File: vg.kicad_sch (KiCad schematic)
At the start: 45 parts, among them J1 Conn_01x07, J2 Conn_01x08, J3 Conn_01x03, Q1 2N7002, Q3 SI2301CDS-T1-GE3, U1 TPS62203DBV, U2 IRLML6344TRPBF, U3 STM32L072CBTx, Y1 32768Hz - 12,5 pF

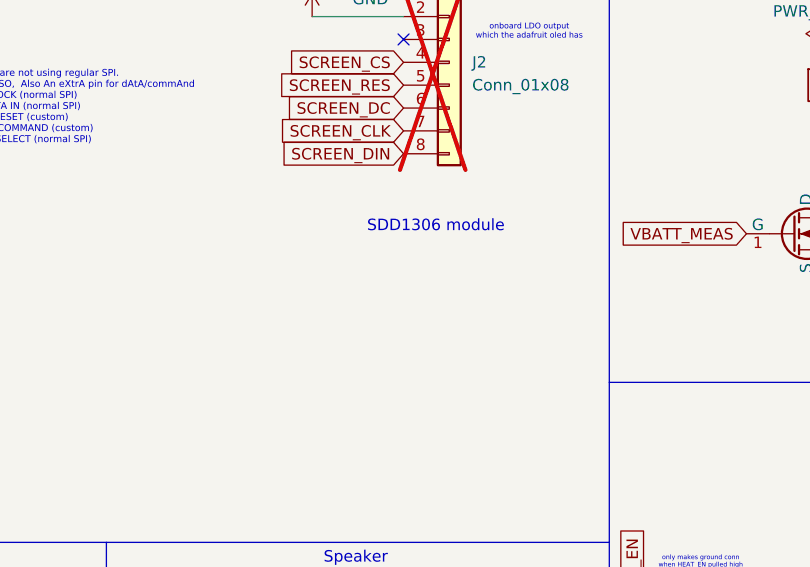
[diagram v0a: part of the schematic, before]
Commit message: add 2nd pin row
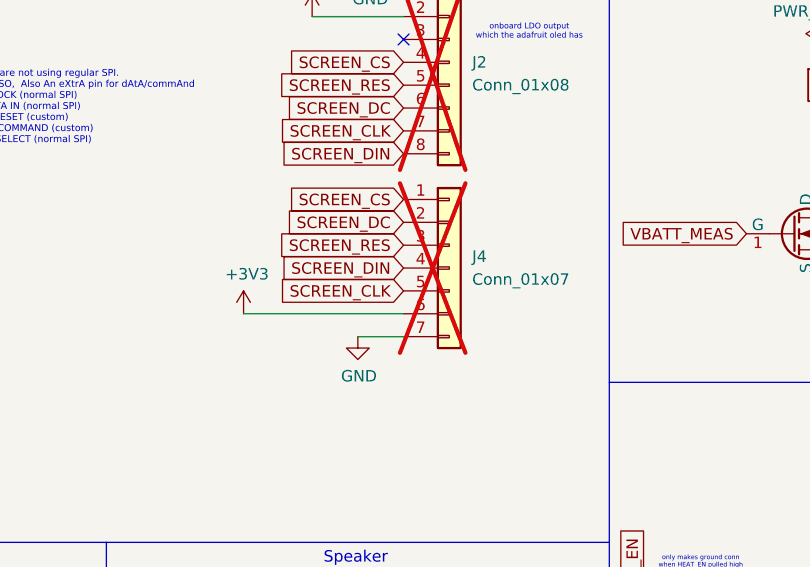
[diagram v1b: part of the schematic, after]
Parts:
- added J4: Conn_01x07, Connector_PinHeader_2.54mm:PinHeader_1x07_P2.54mm_Vertical, symbol Connector_Generic:Conn_01x07
- J2: footprint Connector_PinHeader_2.54mm:PinHeader_1x08_P2.54mm_Horizontal -> Connector_PinHeader_2.54mm:PinHeader_1x08_P2.54mm_Vertical
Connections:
- net +3V3: now also J4.6 (Pin_6)
- net GND: now also J4.7 (Pin_7)
- net SCREEN_CLK: now also J4.5 (Pin_5)
- net SCREEN_CS: now also J4.1 (Pin_1)
- net SCREEN_DC: now also J4.2 (Pin_2)
- net SCREEN_DIN: now also J4.4 (Pin_4)
- net SCREEN_RES: now also J4.3 (Pin_3)
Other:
- note removed: "SDD1306 module"

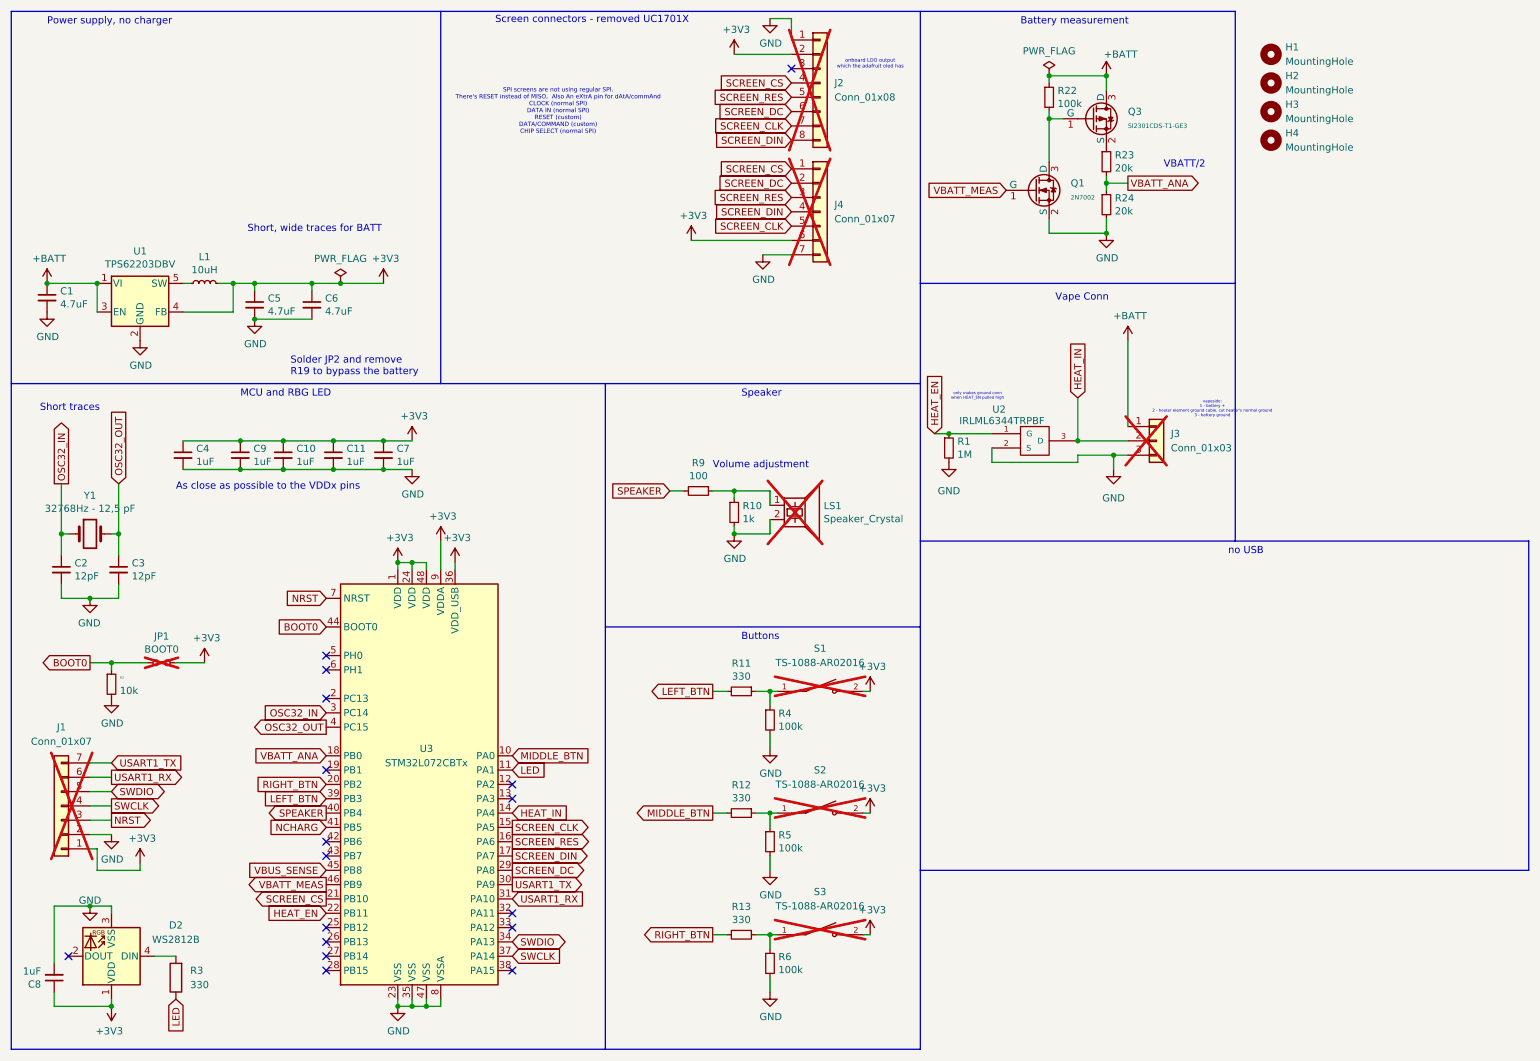
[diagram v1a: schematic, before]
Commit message: dont pour all the way to the edge; replace speaker series cap with 0805 for better thermal; gnd vias on both sides of islands; long trace series resistors close to chip; shorter filter cap connections
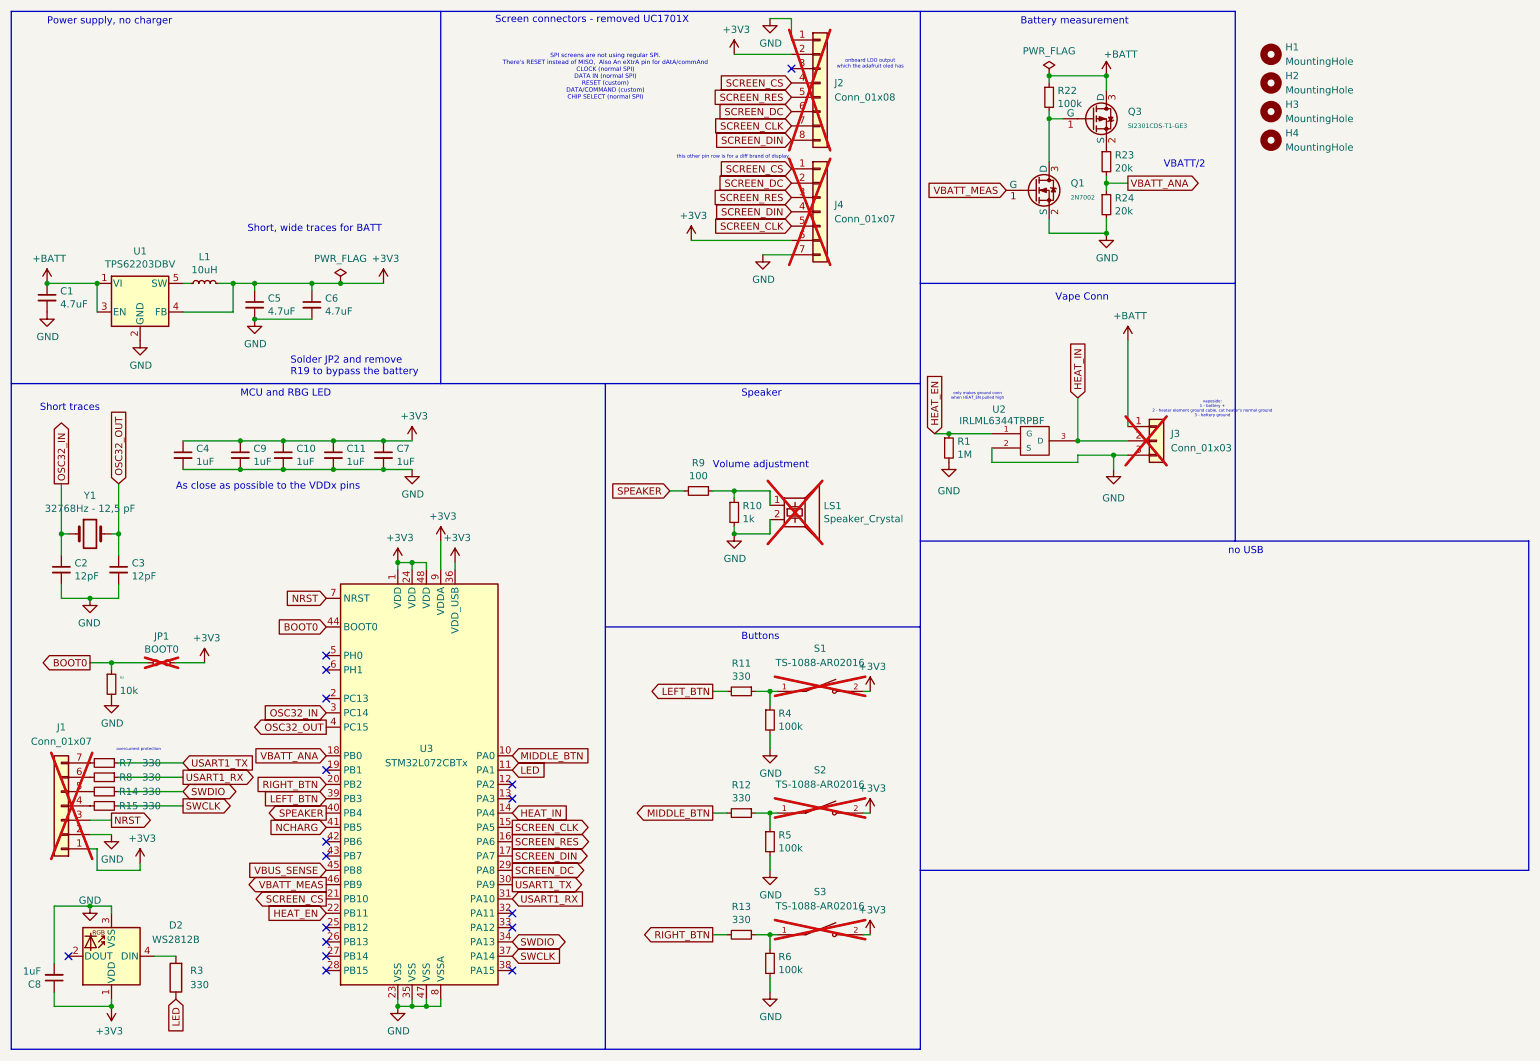
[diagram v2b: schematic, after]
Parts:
- added R14, R15, R7, R8: 330, Resistor_SMD:R_0402_1005Metric, symbol Device:R_Small
- R10: footprint Resistor_SMD:R_0402_1005Metric -> PCM_JLCPCB:R_0402; LCSC C11702 -> (none)
- R9: footprint Resistor_SMD:R_0402_1005Metric -> PCM_JLCPCB:R_0805
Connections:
- net SWCLK: now also R15.1; no longer J1.4 (Pin_4)
- net SWDIO: now also R14.1; no longer J1.5 (Pin_5)
- net USART1_RX: now also R8.1; no longer J1.6 (Pin_6)
- net USART1_TX: now also R7.1; no longer J1.7 (Pin_7)
- new net: J1.7 (Pin_7), R7.2
- new net: J1.5 (Pin_5), R14.2
- new net: J1.6 (Pin_6), R8.2
- new net: J1.4 (Pin_4), R15.2
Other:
- note added: "overcurrent protection"
- note added: "this other pin row is for a diff brand of display"

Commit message: fix some LCSC #s
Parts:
- R9: LCSC C25076 -> C3202623
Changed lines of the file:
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@@
 			)
 		)
-		(property "LCSC" "C25076"
+		(property "LCSC" "C3202623"
 			(at 135.89 97.79 0)
 			(effects
